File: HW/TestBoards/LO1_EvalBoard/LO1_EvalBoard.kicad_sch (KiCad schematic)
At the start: 21 parts, among them J1 SMA, J2 Conn_01x05, U1 MS-156C, U2 CY2-44+, U3 HMC516, Y1 HMC506LP4

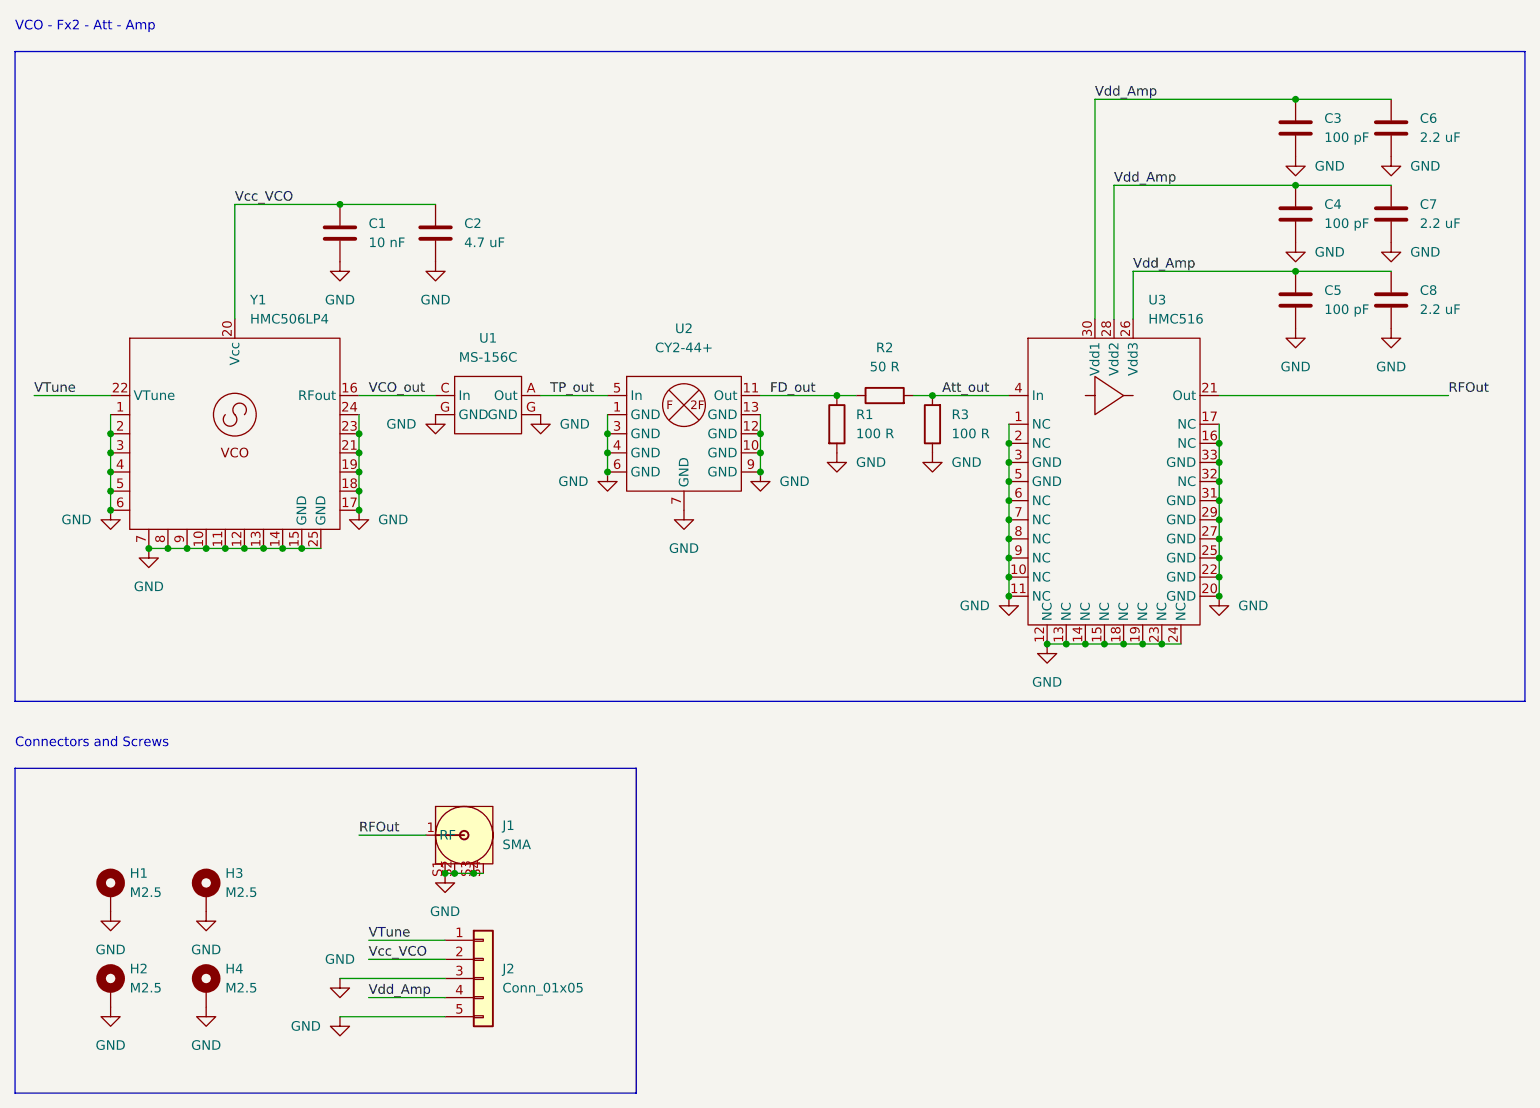
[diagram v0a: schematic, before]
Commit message: All Test Boards developed
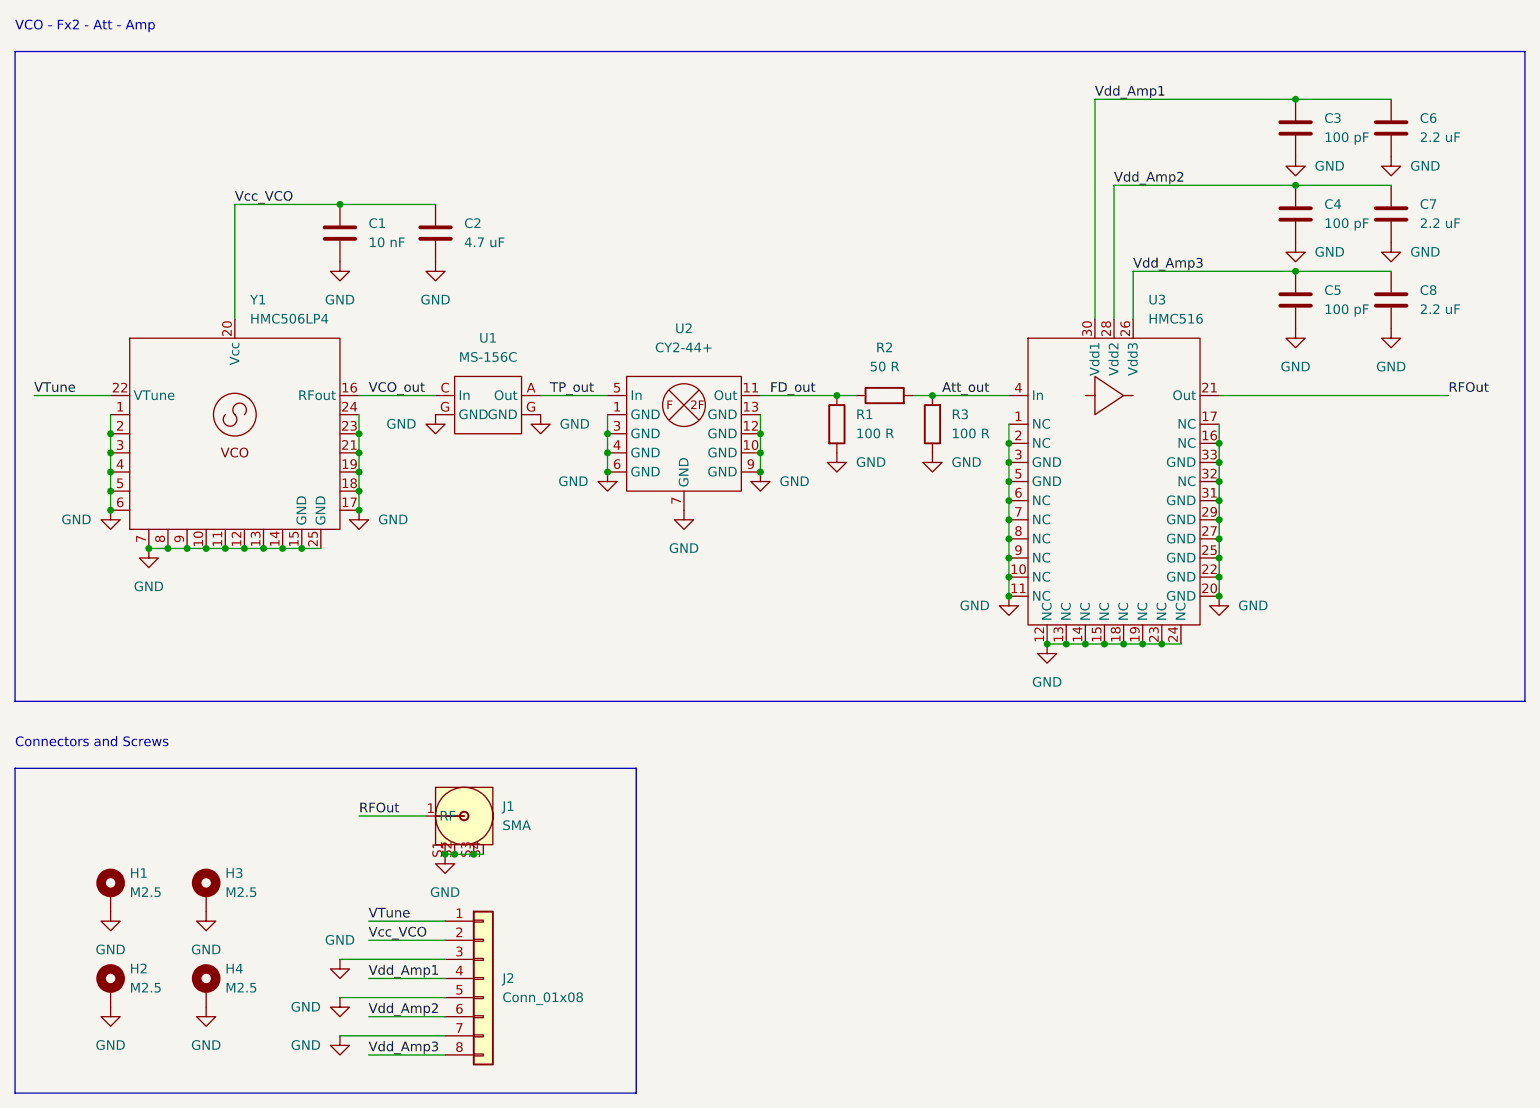
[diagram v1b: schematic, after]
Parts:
- removed J2: Conn_01x05, Connector_PinSocket_2.00mm:PinSocket_1x05_P2.00mm_Vertical, symbol Connector_Generic:Conn_01x05
- added J2: Conn_01x08, Connector_PinSocket_2.00mm:PinSocket_1x08_P2.00mm_Vertical, symbol Connector_Generic:Conn_01x08
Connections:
- net GND: now also J2.3 (Pin_3), J2.5 (Pin_5), J2.7 (Pin_7)
- net VTune: now also J2.1 (Pin_1)
- net Vcc_VCO: now also J2.2 (Pin_2)
- removed net Vdd_Amp: C3.1, C4.1, C5.1, C6.1, C7.1, C8.1, U3.26 (Vdd3), U3.28 (Vdd2), U3.30 (Vdd1)
- new net Vdd_Amp1: C3.1, C6.1, J2.4 (Pin_4), U3.30 (Vdd1)
- new net Vdd_Amp2: C4.1, C7.1, J2.6 (Pin_6), U3.28 (Vdd2)
- new net Vdd_Amp3: C5.1, C8.1, J2.8 (Pin_8), U3.26 (Vdd3)
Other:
- moved on the sheet: J1
